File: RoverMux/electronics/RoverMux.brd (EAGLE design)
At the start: 33.5 x 21.6 mm, 24 parts, among them J1 ISP, U1 TINY13, U2 MCP1824T, U3 74LS157D

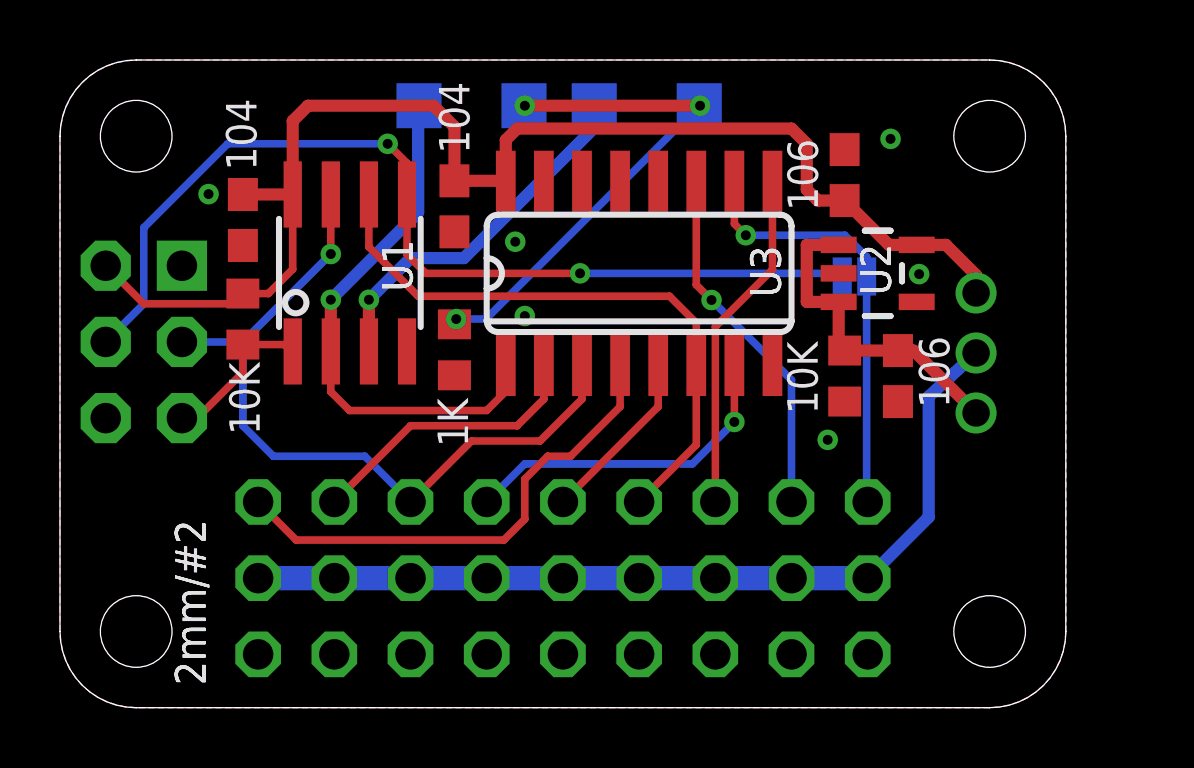
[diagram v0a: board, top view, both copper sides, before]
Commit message: Revised for AVRISP female fitment
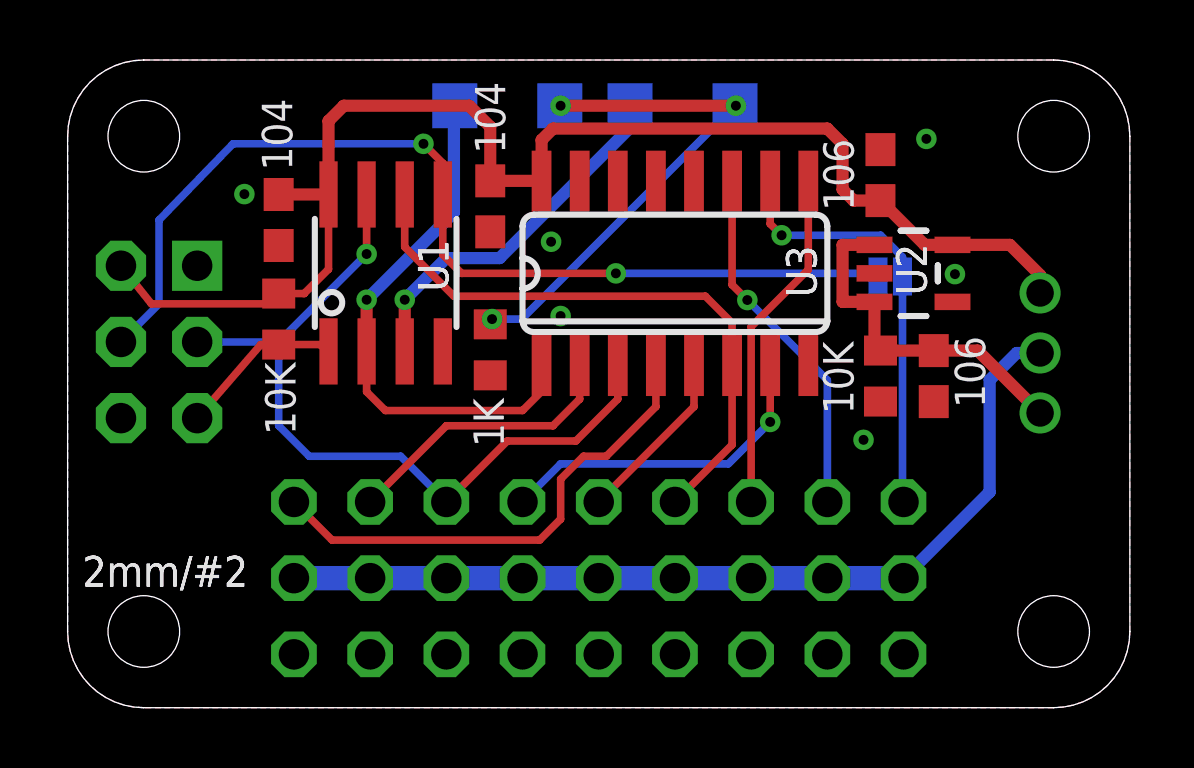
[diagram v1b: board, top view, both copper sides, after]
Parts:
- moved JP1 2.13 mm to (32.4, 11.8)
- moved C5 1.19 mm to (27.1, 17.8)
- moved LED1 1.19 mm to (20.5, 20.1)
- moved U1 1.19 mm to (10.6, 14.5)
- moved C2 1.19 mm to (7.04, 16.3)
- moved JP31 1.19 mm to (7.54, 4.32)
- moved R1 1.19 mm to (7.04, 13.0)
- moved C3 1.19 mm to (28.9, 11.1)
- moved C4 1.19 mm to (14.1, 16.7)
- moved JP11 1.19 mm to (10.1, 4.32)
- moved JP12 1.19 mm to (17.7, 4.32)
- moved JP13 1.19 mm to (25.3, 4.32)
- moved JP21 1.19 mm to (12.6, 4.32)
- moved JP22 1.19 mm to (20.2, 4.32)
- moved JP23 1.19 mm to (27.9, 4.32)
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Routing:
- net +5V: track 44.0 -> 45.7 mm
- net REGIN: track 11.2 -> 12.1 mm
- net MOSI: track 32.4 -> 33.2 mm
- net +7V: track 29.4 -> 30.2 mm
- net CH1RX: track 25.8 -> 26.5 mm
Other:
- board size 33.5 x 21.6 mm -> 35.4 x 21.6 mm
- board text removed: "1"

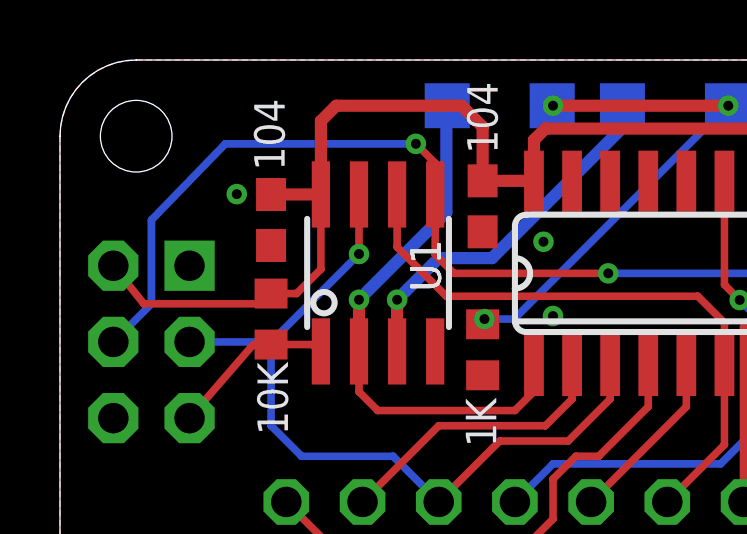
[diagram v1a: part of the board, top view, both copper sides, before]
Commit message: RoverMux electronics changes, minor software changes
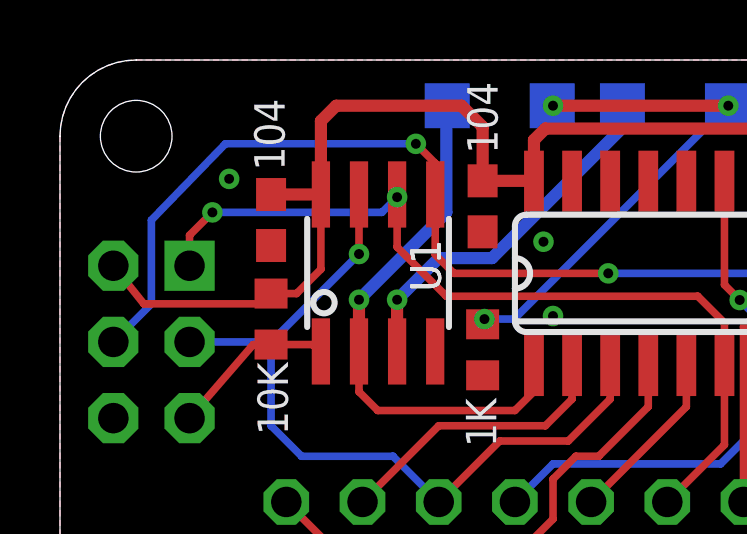
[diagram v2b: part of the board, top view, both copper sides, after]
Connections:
- removed net MISO: J1.1
- net CH2RX: now also J1.1
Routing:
- net CH2RX: track 20.5 -> 28.9 mm, vias 0 -> 2
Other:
- board text added: "R0.4"
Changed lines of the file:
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@@
 <layer number="19" name="Unrouted" color="6" fill="1" visible="yes" active="yes"/>
 <layer number="20" name="Dimension" color="15" fill="1" visible="yes" active="yes"/>
-<layer number="21" name="tPlace" color="7" fill="1" visible="no" active="yes"/>
-<layer number="22" name="bPlace" color="7" fill="1" visible="no" active="yes"/>
+<layer number="21" name="tPlace" color="7" fill="1" visible="yes" active="yes"/>
+<layer number="22" name="bPlace" color="7" fill="1" visible="yes" active="yes"/>
 <layer number="23" name="tOrigins" color="15" fill="1" visible="no" active="yes"/>
 <layer number="24" name="bOrigins" color="15" fill="1" visible="no" active="yes"/>
-<layer number="25" name="tNames" color="7" fill="1" visible="no" active="yes"/>
-<layer number="26" name="bNames" color="7" fill="1" visible="no" active="yes"/>
+<layer number="25" name="tNames" color="7" fill="1" visible="yes" active="yes"/>
+<layer number="26" name="bNames" color="7" fill="1" visible="yes" active="yes"/>
 <layer number="27" name="tValues" color="7" fill="1" visible="no" active="yes"/>
 <layer number="28" name="bValues" color="7" fill="1" visible="no" active="yes"/>
@@
 <text x="33.3756" y="15.494" size="1.016" layer="22" font="vector" rot="MR0">BEC</text>
 <hole x="2.54" y="19.05" drill="2.3876"/>
-<text x="34.6306" y="4.914" size="1.27" layer="26" font="vector" rot="MR0">R0.3</text>
+<text x="34.6306" y="4.914" size="1.27" layer="26" font="vector" rot="MR0">R0.4</text>
 <text x="33.9471" y="8.9535" size="1.016" layer="22" font="vector" rot="MR90">6V | 5V</text>
 <text x="0.5" y="4.04" size="1.016" layer="21" font="vector">2mm/#2</text>
@@
 <attribute name="PARTNO" value="CL10A106MP8NNNC" x="28.8718" y="11.054" size="1.778" layer="27" rot="R270" display="off"/>
 <attribute name="VALUE" x="29.5703" y="12.3875" size="1.016" layer="27" font="vector" rot="R270"/>
+<attribute name="VOLTAGE" value="10V" x="28.8718" y="11.054" size="1.778" layer="27" rot="R270" display="off"/>
 </element>
 <element name="U3" library="74xx-us" package="SO16" value="74LS157D" x="20.2438" y="14.478" smashed="yes">
@@
 <via x="28.6253" y="18.961" extent="1-16" drill="0.3302"/>
 <via x="26.5298" y="8.928" extent="1-16" drill="0.3302"/>
-<via x="5.8923" y="17.1195" extent="1-16" drill="0.3302"/>
+<via x="5.6383" y="17.6275" extent="1-16" drill="0.3302"/>
 </signal>
 <signal name="CH2RX">
@@
 <wire x1="22.1488" y1="11.4046" x2="22.1488" y2="8.763" width="0.254" layer="1"/>
 <wire x1="22.1488" y1="8.763" x2="20.2438" y2="6.858" width="0.254" layer="1"/>
-<wire x1="11.2368" y1="17.1082" x2="11.2368" y2="15.357" width="0.254" layer="1"/>
+<wire x1="11.2368" y1="17.1082" x2="11.2368" y2="17.018" width="0.254" layer="1"/>
+<wire x1="11.2368" y1="17.018" x2="11.2368" y2="15.357" width="0.254" layer="1"/>
 <wire x1="11.2368" y1="15.357" x2="12.8778" y2="13.716" width="0.254" layer="1"/>
 <wire x1="12.8778" y1="13.716" x2="21.2598" y2="13.716" width="0.254" layer="1"/>
 <wire x1="22.1488" y1="11.4046" x2="22.1488" y2="12.827" width="0.254" layer="1"/>
 <wire x1="22.1488" y1="12.827" x2="21.2598" y2="13.716" width="0.254" layer="1"/>
+<contactref element="J1" pad="1"/>
+<wire x1="4.318" y1="14.732" x2="4.318" y2="15.748" width="0.254" layer="1"/>
+<wire x1="4.318" y1="15.748" x2="5.08" y2="16.51" width="0.254" layer="1"/>
+<via x="5.08" y="16.51" extent="1-16" drill="0.3302"/>
+<wire x1="5.08" y1="16.51" x2="10.7288" y2="16.51" width="0.254" layer="16"/>
+<wire x1="10.7288" y1="16.51" x2="11.2368" y2="17.018" width="0.254" layer="16"/>
+<via x="11.2368" y="17.018" extent="1-16" drill="0.3302"/>
 </signal>
 <signal name="CH3RX">
@@
 <wire x1="15.1358" y1="12.954" x2="22.2478" y2="20.066" width="0.254" layer="16"/>
 </signal>
-<signal name="MISO">
-<contactref element="J1" pad="1"/>
-</signal>
 </signals>

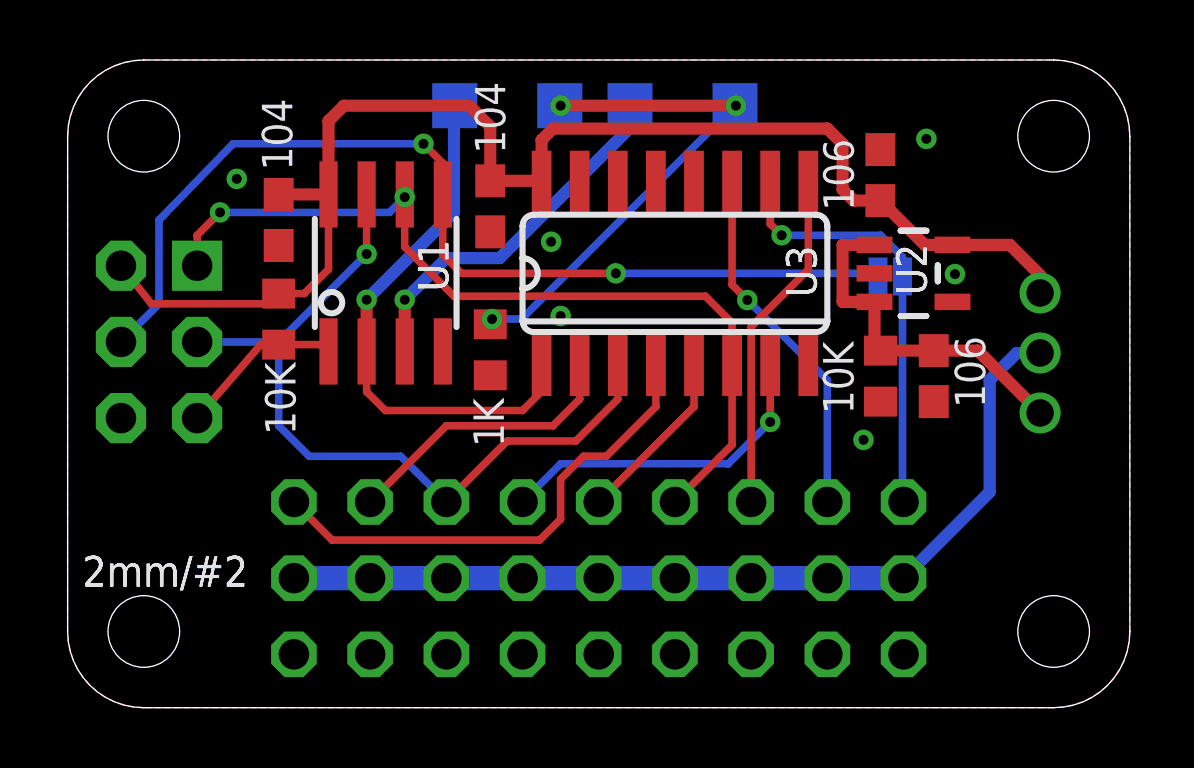
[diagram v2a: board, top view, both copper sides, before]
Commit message: Revised 8SOIC footprint, replaced 5V regulator and selector with 3.3V regulator to simplify. Moved devices around, simplified routing to pin headers. Placed missing ISP trace. Revised schematic layout.
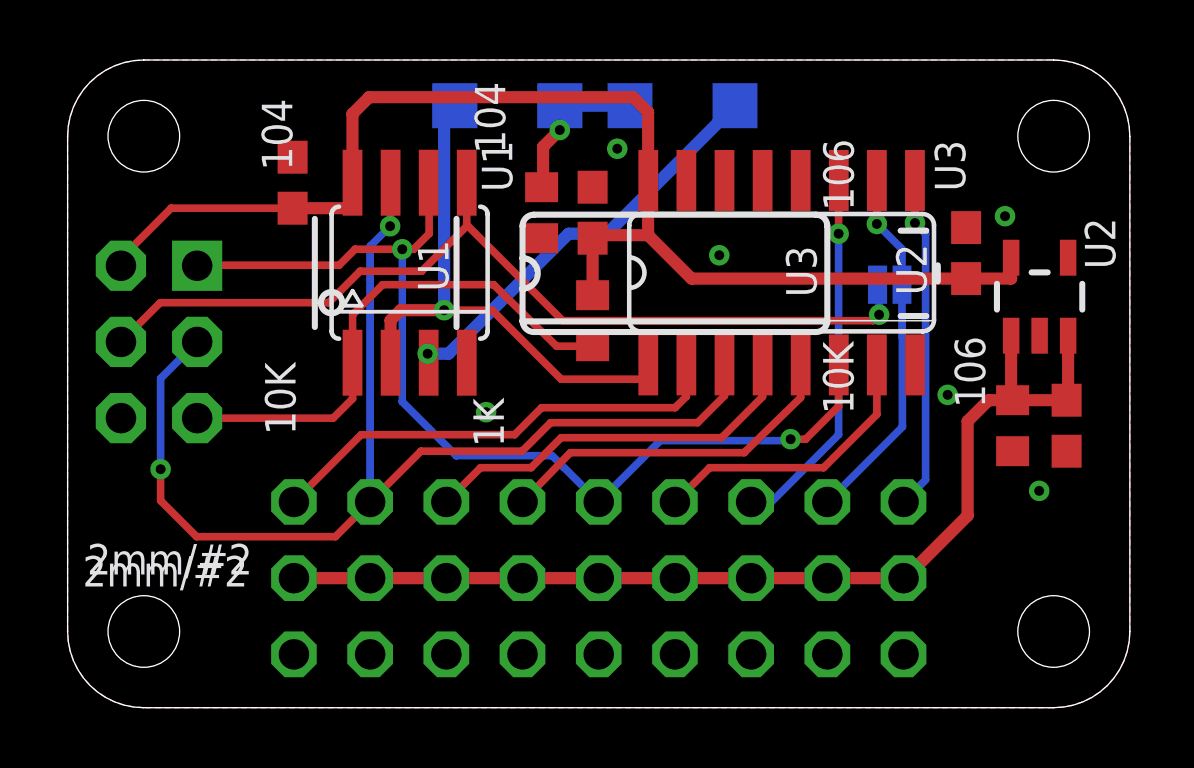
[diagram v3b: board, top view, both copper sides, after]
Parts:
- removed JP1: PWRSEL, pinhead-2:1X03M
- U1: value TINY13 -> TINY25/45/85-20SU; device avr-7:SO08 -> bt_avr:SOIC8
- U3: value 74LS157D -> 74HC157D
- moved C2 10.5 mm to (17.5, 16.5), turned to 90 degrees
- moved R1 10.5 mm to (17.5, 12.9)
- moved C4 6.63 mm to (7.50, 17.5), turned to 90 degrees
- moved JP33 5.08 mm to (27.9, 4.32)
- moved JP32 5.08 mm to (20.2, 4.32)
- moved JP31 5.08 mm to (12.6, 4.32)
- moved R2 4.88 mm to (15.8, 16.5)
- moved C3 4.73 mm to (33.3, 9.40)
- moved R4 4.70 mm to (31.5, 9.40)
- moved U2 4.28 mm to (32.4, 13.7), turned to 0 degrees
- moved C5 3.86 mm to (29.9, 15.2)
- moved U3 3.56 mm to (23.8, 14.5)
- moved JP23 2.54 mm to (25.3, 4.32)
- moved JP12 2.54 mm to (15.2, 4.32)
- moved JP11 2.54 mm to (7.54, 4.32)
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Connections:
- removed net +5V: C2.1, C4.1, C5.1, J1.2, JP1.1, R1.2, U1.8, U2.5, U3.16
- removed net +7V: JP1.2, JP11.2, JP12.2, JP13.2, JP21.2, JP22.2, JP23.2, JP31.2, JP32.2, JP33.2
- removed net REGIN: C3.1, JP1.3, R4.2, U2.1, U2.3
- new net 3.3V: C2.1, C4.1, C5.1, J1.2, R1.2, U1.8, U2.5, U3.16
- new net BEC: C3.1, JP11.2, JP12.2, JP13.2, JP21.2, JP22.2, JP23.2, JP31.2, JP32.2, JP33.2, R4.2, U2.1, U2.3
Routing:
- net +5V: track 45.7 -> 0.00 mm
- net 3.3V: track 0.00 -> 43.9 mm
- net BEC: track 0.00 -> 34.8 mm
- net +7V: track 30.2 -> 0.00 mm
- net CH1RX: track 26.5 -> 39.0 mm, vias 1 -> 2
- net REGIN: track 12.1 -> 0.00 mm
- net N$3: track 17.3 -> 5.31 mm, vias 3 -> 1
- net !RESET: track 5.58 -> 17.5 mm
- net CH1MCU: track 9.52 -> 15.6 mm
- net CH2MCU: track 5.86 -> 11.8 mm
- net CH2RX: track 28.9 -> 33.6 mm
- net CH1OUT: track 16.6 -> 13.1 mm
- net MOSI: track 33.2 -> 30.7 mm, vias 2 -> 1
- net CH3RX: track 14.5 -> 12.1 mm
- net A: track 12.3 -> 14.0 mm
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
